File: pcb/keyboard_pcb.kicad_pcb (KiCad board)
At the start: 2 copper layers, 138.8 x 89.9 mm, 23 parts, among them J1 TRRS, K00 KEYSW, K01 KEYSW, K02 KEYSW, K03 KEYSW, K04 KEYSW, K05 KEYSW, K10 KEYSW, K11 KEYSW, K12 KEYSW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

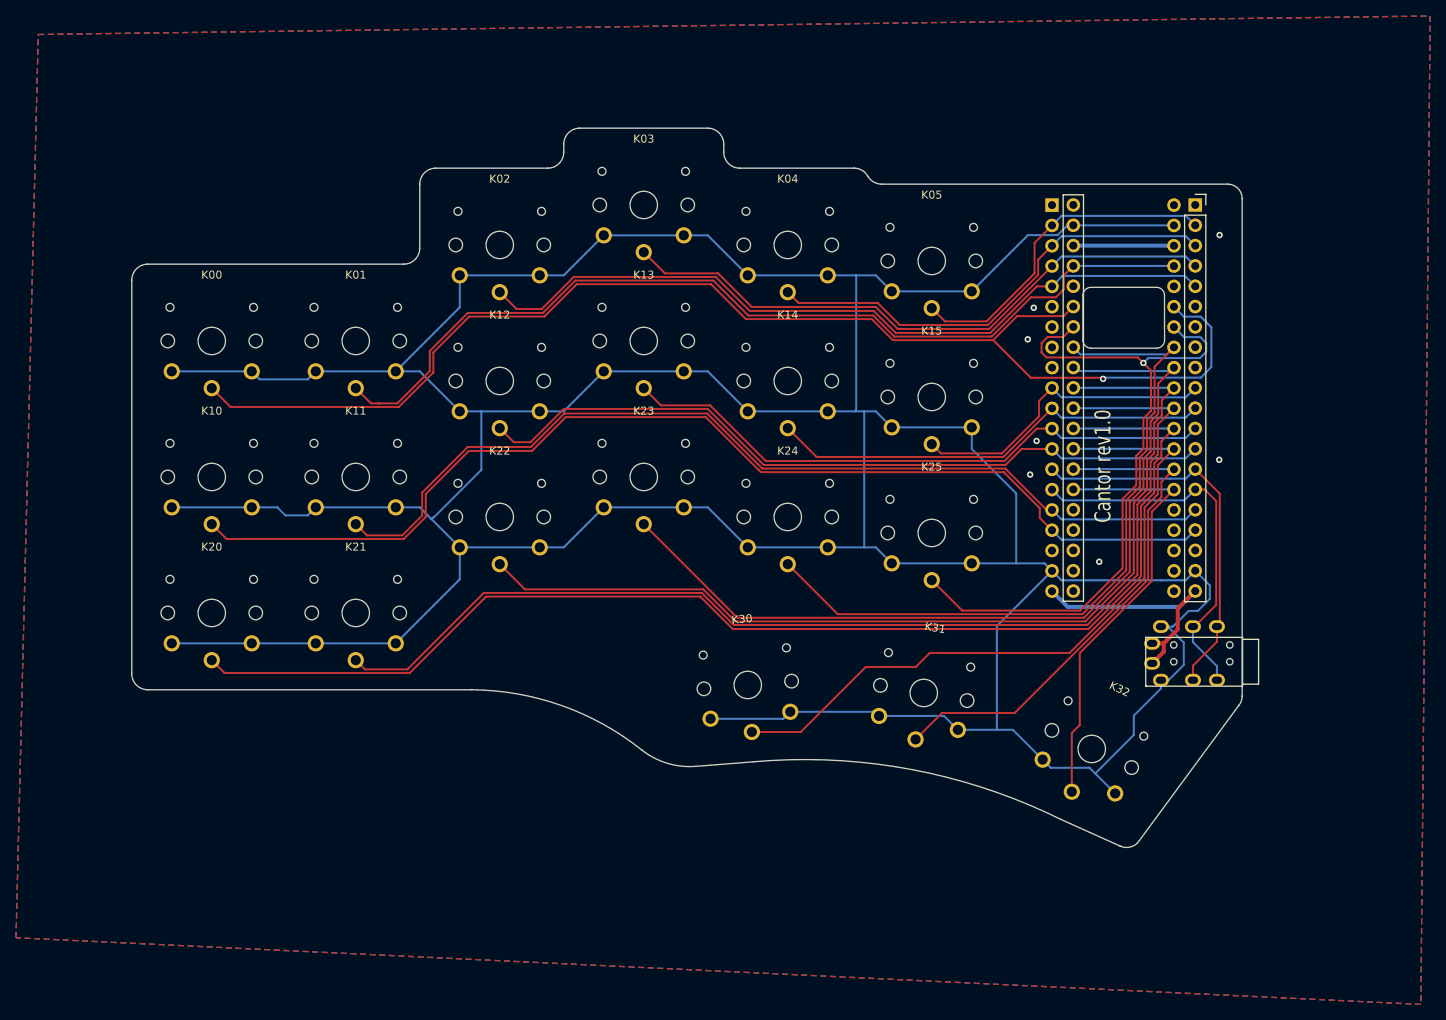
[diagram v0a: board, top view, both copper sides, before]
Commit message: Add holes for the brass standoffs
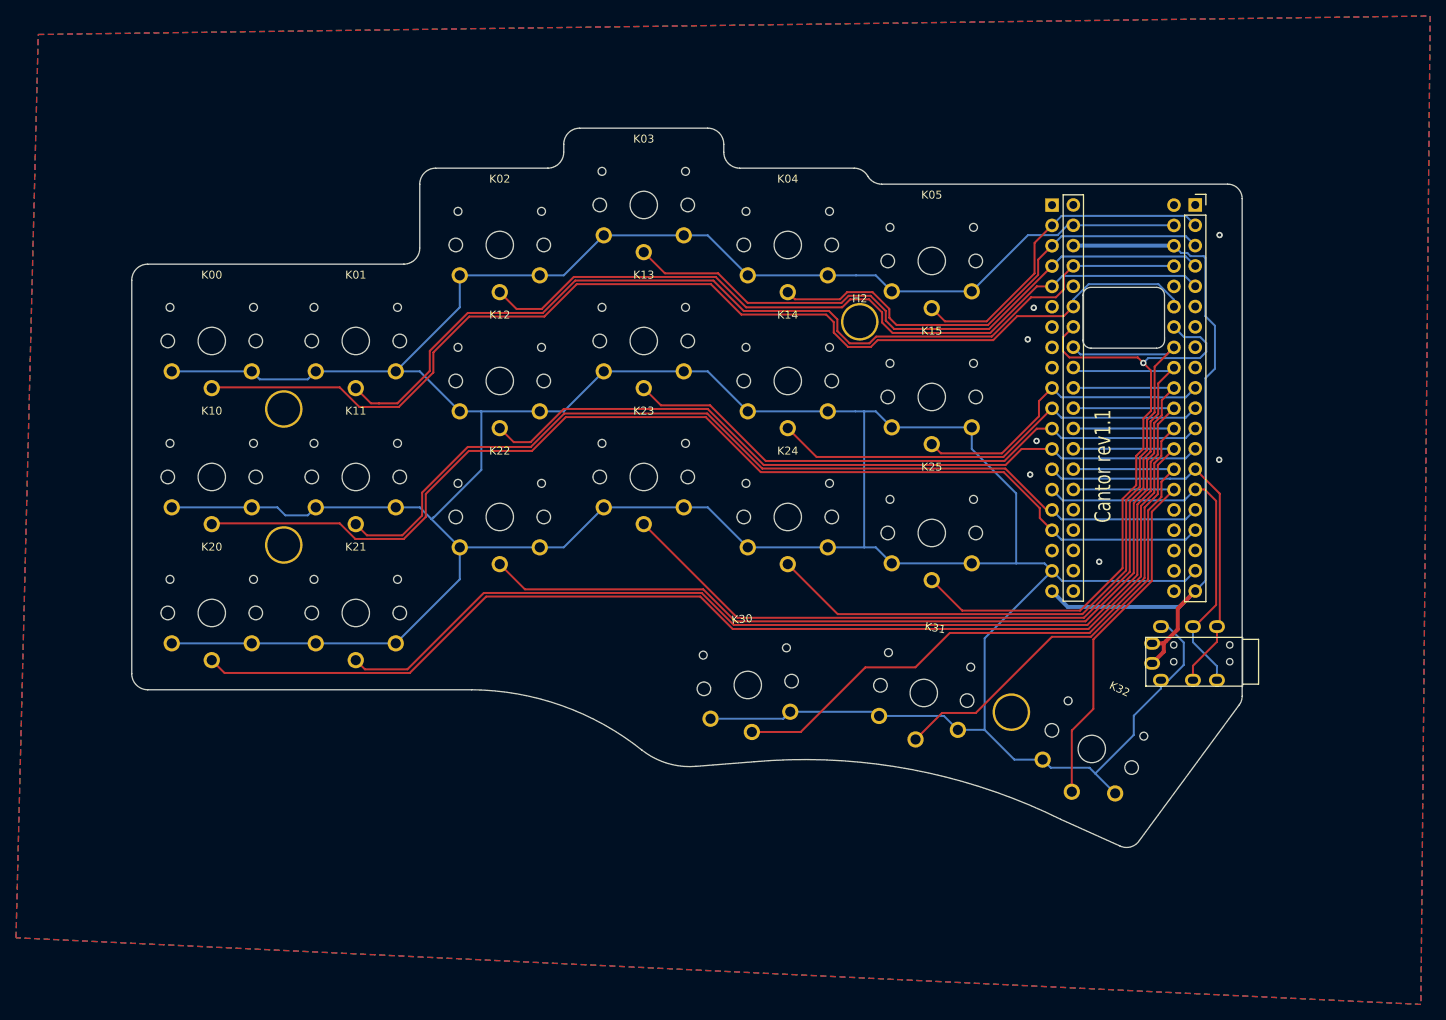
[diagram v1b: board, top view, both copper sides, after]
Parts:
- added H1: MountingHole, cantor:Standoff_Hole, F.Cu at (83.0, 78.5)
- added H2: MountingHole, cantor:Standoff_Hole, F.Cu at (155.0, 67.6)
- added H3: MountingHole, cantor:Standoff_Hole, F.Cu at (83.0, 95.5)
- added H4: MountingHole, cantor:Standoff_Hole, F.Cu at (173.9, 116.4)
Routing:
- net +3V3: track 44.8 -> 92.6 mm
- net GND: track 586.2 -> 558.1 mm
- net /k00: track 161.7 -> 138.6 mm, vias 1 -> 0
- net /k25: track 88.8 -> 83.8 mm
- net /k02: track 95.8 -> 97.4 mm
- net /k01: track 118.5 -> 120.0 mm
- net /k03: track 77.1 -> 78.6 mm
- net /k04: track 58.8 -> 60.2 mm
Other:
- board text added: "Cantor rev1.1"
- board text removed: "Cantor rev1.0"
